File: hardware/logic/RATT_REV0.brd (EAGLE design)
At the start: 109.3 x 76.2 mm, 104 parts, among them J1 0472192001, J2 F-1X02-SIP-100-40, J3 F-1X06-SIP-100-40, J4 F-1X07-SIP-100-40, J5 F-1X02-SIP-100-40, J6 F-1X05-SIP-100-40, Q1 2.5A/30V, Q2 MBT3904DW1T1, Q5 2N7002, U1 ESP-WROOM-32, U3 MCP73831, U4 FT231XS, U5 AP2112K-3.3V, U6 PCA9539PW

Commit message: Bye bye ESP, hello pi
Removed all the old ESP stuff, added some power path stuff, conencted nets to the pi pins renaming as needed.  Mucho cleanup needed.
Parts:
- removed C11, C14, C16: 0.1uF, SparkFun-Capacitors:0603
- removed C12, C13: 47pF, SparkFun-Capacitors:0603
- removed C15: 4.7uF, SparkFun-Capacitors:0603-CAP
- removed C4: 0.1uF, SparkFun-Passives:0603-CAP
- removed D2: BAT20J, SparkFun-DiscreteSemi:SOD-323
- removed J1: 0472192001, DURRIDGE:USD
- removed J2: F-1X02-SIP-100-40, con-headers-jp:SIP-100-02-40
- removed J6: F-1X05-SIP-100-40, con-headers-jp:SIP-100-05-40
- removed JP15: (no value), SparkFun-Connectors:USB-B-MICRO-SMD_V03
- removed R13, R14: 51K, SparkFun-Passives:0603-RES
- removed R15, R16: 27, SparkFun-Resistors:0603
- removed R2, R3, R4: 100R, SparkFun-Resistors:0603-RES
- removed R22, R23: 10k, SparkFun-Resistors:0603
- removed SW4: (no value), MakeIt_Labs:ESWITCH320
- removed U1: ESP-WROOM-32, esp32:ESP-WROOM-32
- removed U4: FT231XS, SparkFun-DigitalIC:SSOP20_L
- added Q3, Q6: 2.5A/30V, SparkFun-DiscreteSemi:SOT23-3
- added Q4, Q7: (no value), DURRIDGE-TRANSISTORS:SOT23-3
- added R36: 1K, SparkFun-Resistors:0603
- added SW0: (no value), MakeIt_Labs:ESWITCH320
- R1: value 100R -> 0R; device SparkFun-Resistors:0603-RES -> SparkFun-Passives:0603-RES
- R10, R11: value 51K -> 10k; device SparkFun-Passives:0603-RES -> SparkFun-Resistors:0603
- R12, R9: value 51K -> 1k; device SparkFun-Passives:0603-RES -> SparkFun-Resistors:0603
- moved R1 473.9 mm to (-173.7, -204.2)
- moved R9 471.8 mm to (-173.7, -197.9)
- moved R10 470.3 mm to (-173.7, -201.2)
- moved R12 455.2 mm to (-167.6, -194.6)
- moved R11 454.1 mm to (-164.6, -191.3)
- moved SW2 12.7 mm to (80.6, 31.8)
- moved SW3 12.7 mm to (80.6, 19.1)
- moved SW1 12.7 mm to (80.6, 44.5)
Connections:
- removed net 3.3V_F: C16.1, U4.13, U4.14, U4.3
- removed net BOOTLOADER: Q2.6, U1.25
- removed net D+: C13.1, JP15.D+, R16.1
- removed net D-: C12.1, JP15.D-, R15.1
- removed net DTR: J6.4, Q2.1, R22.1, U4.1
- removed net N$13: Q2.5, R22.2
- removed net N$15: Q2.2, R23.2
- removed net N$19: R25.1, U6.1
- removed net N$20: R32.1, SW2.3, U1.5
- removed net N$23: R33.1, SW3.3, U1.6
- removed net N$24: R34.1, SW4.3, U1.7
- removed net N$25: R31.1, SW1.3, U1.4
- removed net RFID_RXD: U1.27
- removed net RTS: J6.5, Q2.4, R23.1, U4.2
- removed net RXD0: J6.3, U1.34, U4.20
- removed net SD_CLK: J1.5, R1.2, R14.2, U1.13
- removed net SD_CMD: J1.3, R10.1, R4.2, U1.23
- removed net SD_D0: J1.7, R11.1, U1.24
- removed net SD_D1: J1.8, R13.1, U1.26
- removed net SD_D2: J1.1, R12.1, R2.2, U1.14
- removed net SD_D3: J1.2, R3.2, R9.1, U1.16
- removed net SPI_MISO: SJ10.2, U1.31
- removed net SPI_MOSI: SJ8.2, U1.37
- removed net SPI_SCK: SJ9.2, U1.30
- removed net SPI_TFT_CS0: SJ7.2, U1.29
- removed net TFT_BACKLIGHT: SJ11.2, U1.9
- removed net TFT_DAT/COM: SJ6.2, U1.12
- removed net TFT_RESET: R30.1, SJ5.2, U1.8, U6.3
- removed net TXD0: J6.2, U1.35, U4.4
- new net !BUTTON0: R31.1, SW0.3, U$1.31
- new net !BUTTON1: R32.1, SW1.3, U$1.26
- new net !BUTTON2: R33.1, SW2.3, U$1.32
- new net !BUTTON3: R34.1, SW3.3, U$1.33
- new net !I/O_IRQ: R25.1, U$1.7, U6.1
- new net !I/O_RESET: R30.1, U6.3
- new net !LED0: U$1.29
- new net !SHUTDOWN: R12.1, U$1.13
- new net +5V: C19.1, Q1.1, Q6.3, R17.2, R18.1, R9.2, U3.4
- new net 3V3@2: R1.1, U$1.1, U$1.17
- new net CHARGE_STATUS: D1.C, R36.2, U3.1
- new net GND@3: U$1.25, U$1.39, U$1.9
- new net GND@6: U$1.14, U$1.20, U$1.30, U$1.34, U$1.6
- new net LCD_BACKLIGHT: SJ11.2, U$1.16
- new net LCD_CS: SJ7.2, U$1.24
- new net LCD_D/C: SJ6.2, U$1.18
- new net LCD_MISO: SJ10.2, U$1.21
- new net LCD_MOSI: SJ8.2, U$1.19
- new net LCD_RESET: SJ5.2, U$1.22
- new net LCD_SCK: SJ9.2, U$1.23
- new net N$35: Q7.1, R9.1
- new net N$36: U$1.36
- new net N$37: Q3.1, Q4.3, R11.1
- new net N$38: Q4.1, R12.2
- new net N$39: U$1.15
- new net N$40: U$1.11
- new net PWR_LOSS: U$1.37
- net +3V3: now also R1.2; no longer C1.1, C17.1, C2.1, C4.1, C9.1, J1.4, R10.2, R11.2, R12.2, R13.2, R5.2, R7.2, R9.2, U1.2, U2.7, U2.8
- net 3.3V: now also R36.1
- net GND: now also Q4.2, Q7.2, SW0.1; no longer C1.2, C11.2, C12.2, C13.2, C14.2, C15.2, C16.2, C4.2, J1.6, J1.G1, J1.G2, J1.G3, J1.G4, J2.2, J6.1, JP15.GND, JP15.SHIELD1, JP15.SHIELD2, JP15.SHIELD3, R14.1, SW4.1, U1.1, U1.15, U1.38, U1.GND, U4.16, U4.6
- net I2C_SCL: now also U$1.5; no longer U1.36
- net I2C_SDA: now also U$1.3; no longer U1.33
- net I2S_BCK: now also U$1.12; no longer U1.11
- net I2S_DOUT: now also U$1.40; no longer U1.28
- net I2S_WS/LRCLK: now also U$1.35; no longer U1.10
- net JTAG_TCK: no longer R3.1
- net JTAG_TDI: no longer R2.1
- net JTAG_TDO: no longer R4.1
- net JTAG_TMS: no longer R1.1
- net N$10: now also Q1.3, Q3.3; no longer D1.C, U3.1
- net N$8: now also C2.1, R5.2; no longer R15.2, U4.12
- net N$9: now also Q6.1, Q7.3, R10.2; no longer R16.2, U4.11
- net RFID_RX: now also U$1.10
- net RFID_TX: now also U$1.8
- net VIN: now also C17.1, C9.1, Q6.2, R10.1, R7.2, U$1.2, U$1.4, U2.7, U2.8; no longer D2.C
- net VUSB-RAW: no longer C11.1, J2.1, JP15.VBUS
- net V_BATT: now also Q3.2, R11.2; no longer Q1.3
- net V_USB: no longer C14.1, C15.1, C19.1, D2.A, Q1.1, R17.2, R18.1, U3.4, U4.15
- net ~RESET: no longer Q2.3, R5.1, U1.3
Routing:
- net SD_CLK: track 32.5 -> 0.00 mm
- net SD_D1: track 26.5 -> 0.00 mm
- net SD_D2: track 21.0 -> 0.00 mm
- net SD_CMD: track 18.8 -> 0.00 mm
- net SD_D3: track 17.7 -> 0.00 mm
- net SD_D0: track 17.5 -> 0.00 mm
- net N$8: track 14.4 -> 0.00 mm
- net N$9: track 10.7 -> 0.00 mm
- net 3.3V_F: track 8.49 -> 0.00 mm
- net RXD0: track 8.48 -> 0.00 mm
- net +3V3: track 9.02 -> 1.52 mm
- net D+: track 5.82 -> 0.00 mm
- net D-: track 5.23 -> 0.00 mm
- net VIN: track 0.00 -> 5.23 mm
- net RTS: track 3.46 -> 0.00 mm
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
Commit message: Forgot to save first
derp
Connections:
- removed net N$40: U$1.11
- net !I/O_RESET: now also U$1.11
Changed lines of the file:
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@@
 <contactref element="U$1" pad="15"/>
-</signal>
-<signal name="N$40">
-<contactref element="U$1" pad="11"/>
 </signal>
 <signal name="!I/O_IRQ">
@@
 <contactref element="U6" pad="3"/>
 <contactref element="R30" pad="1"/>
+<contactref element="U$1" pad="11"/>
 <wire x1="-95.592" y1="-82.55" x2="-111.887" y2="-68.8086" width="0" layer="19" extent="1-1"/>
+<wire x1="-14.394" y1="38.366" x2="-111.887" y2="-68.8086" width="0" layer="19" extent="1-1"/>
 </signal>
 </signals>

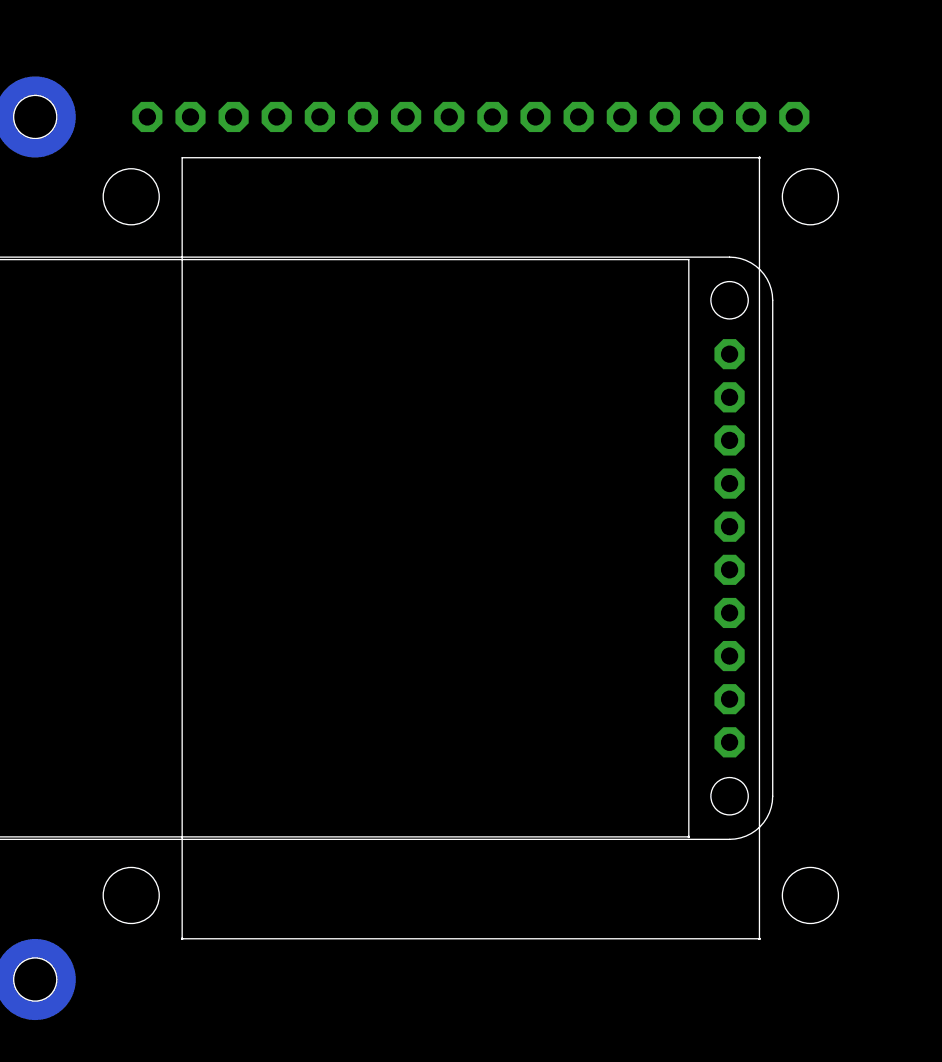
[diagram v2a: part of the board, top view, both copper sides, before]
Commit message: new display, buttons moved
Added chinafruit 2.0, moved buttons to i/o expander, added i/o lines to expander
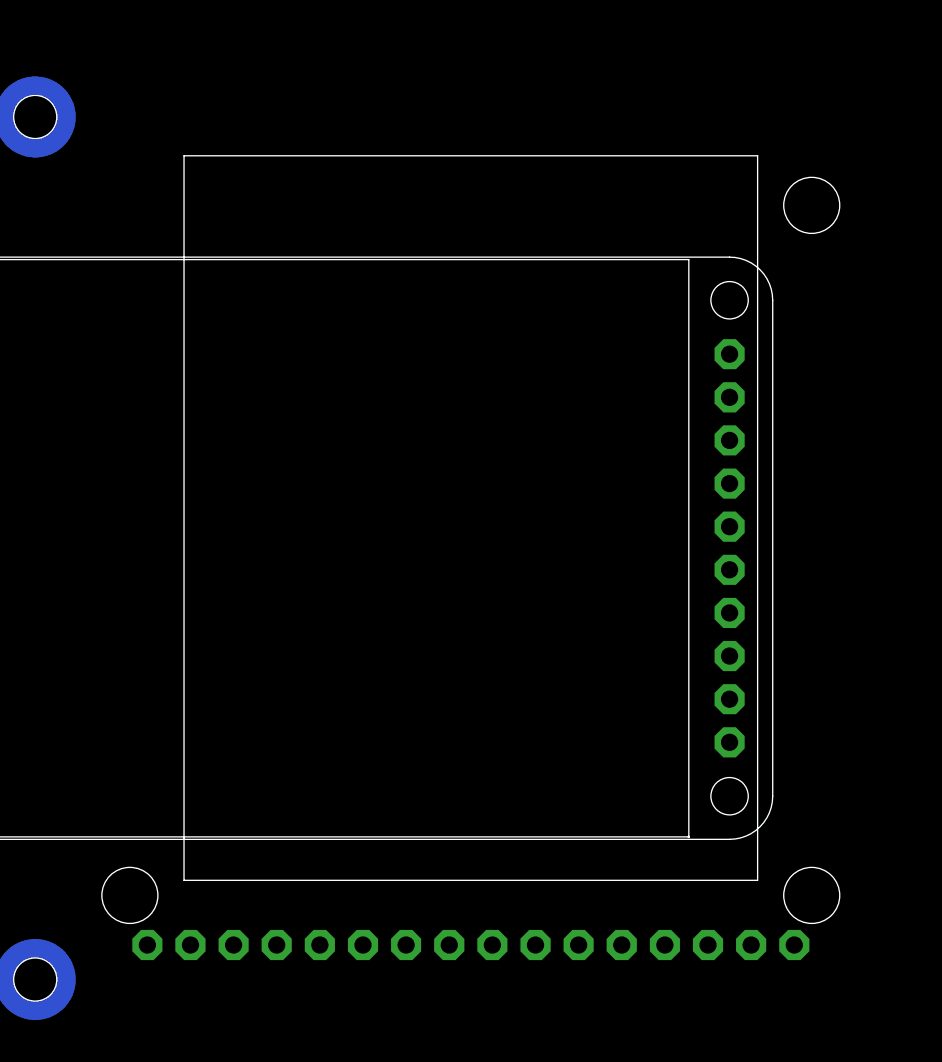
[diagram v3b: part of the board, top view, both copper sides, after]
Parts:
- removed LCD2: 1.8TFT_CHI, MakeIt_Labs:1.8TFT_CHI
- added LCD3: 1.8TFT_CHI2.0, MakeIt_Labs:1.8TFT_CHI_2.0
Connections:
- removed net N$36: U$1.36
- removed net N$39: U$1.15
- new net IN0: U6.4
- new net IN1: U6.5
- new net IN2: U6.6
- new net IN3: U6.7
- new net N$13: U$1.26
- new net OUT0: U6.8
- new net OUT1: U6.9
- new net OUT2: U6.10
- new net OUT3: U6.11
- net !BUTTON0: now also U6.13; no longer U$1.31
- net !BUTTON1: now also U6.14; no longer U$1.26
- net !BUTTON2: now also U6.15; no longer U$1.32
- net !BUTTON3: now also U6.16; no longer U$1.33
- net N$26: now also LCD3.15, LCD3.2; no longer LCD2.15, LCD2.2
- net N$27: now also LCD3.6; no longer LCD2.6
- net N$28: now also LCD3.7; no longer LCD2.7
- net N$29: now also LCD3.10; no longer LCD2.10
- net N$3: now also LCD3.1; no longer LCD2.1
- net N$30: now also LCD3.8; no longer LCD2.8
- net N$31: now also LCD3.9; no longer LCD2.9
- net N$34: now also LCD3.16; no longer LCD2.16
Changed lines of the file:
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@@
 <element name="SJ10" library="SparkFun-Passives" package="PAD-JUMPER-2-NC_BY_TRACE_YES_SILK" value="JUMPER-PAD-2-NC_BY_TRACE" x="-149.8" y="-133.32"/>
 <element name="SJ11" library="SparkFun-Passives" package="PAD-JUMPER-2-NC_BY_TRACE_YES_SILK" value="JUMPER-PAD-2-NC_BY_TRACE" x="-125.9" y="-129.06" rot="R180"/>
-<element name="LCD2" library="MakeIt_Labs" package="1.8TFT_CHI" value="1.8TFT_CHI" x="40.64" y="38.1" rot="MR270"/>
 <element name="J4" library="con-headers-jp" package="SIP-100-07-40" value="F-1X07-SIP-100-40" x="-139.7" y="-144.78"/>
 <element name="C24" library="SparkFun-Capacitors" package="0603-CAP@1" value="0.1uF" x="-152.4" y="-157.48"/>
@@
 </element>
 <element name="R1" library="SparkFun-Passives" package="0603-RES" value="0R" x="-173.736" y="-204.216"/>
+<element name="LCD3" library="MakeIt_Labs" package="1.8TFT_CHI_2.0" value="1.8TFT_CHI2.0" x="40.64" y="14.732" rot="MR90"/>
 </elements>
 <signals>
@@
 <contactref element="SJ3" pad="1"/>
 <contactref element="LCD1" pad="1"/>
-<contactref element="LCD2" pad="1"/>
-<wire x1="59.69" y1="63.5" x2="55.88" y2="49.53" width="0" layer="19" extent="1-1"/>
-<wire x1="-142.708" y1="-118.02" x2="59.69" y2="63.5" width="0" layer="19" extent="1-1"/>
+<contactref element="LCD3" pad="1"/>
+<wire x1="21.59" y1="14.732" x2="55.88" y2="49.53" width="0" layer="19" extent="1-1"/>
+<wire x1="-142.708" y1="-118.02" x2="21.59" y2="14.732" width="0" layer="19" extent="1-1"/>
 </signal>
 <signal name="N$26">
 <contactref element="SJ4" pad="1"/>
 <contactref element="LCD1" pad="2"/>
-<contactref element="LCD2" pad="2"/>
-<contactref element="LCD2" pad="15"/>
-<wire x1="55.88" y1="46.99" x2="24.13" y2="63.5" width="0" layer="19" extent="1-1"/>
-<wire x1="57.15" y1="63.5" x2="55.88" y2="46.99" width="0" layer="19" extent="1-1"/>
-<wire x1="-132.908" y1="-133.32" x2="57.15" y2="63.5" width="0" layer="19" extent="1-1"/>
+<contactref element="LCD3" pad="2"/>
+<contactref element="LCD3" pad="15"/>
+<wire x1="57.15" y1="14.732" x2="55.88" y2="46.99" width="0" layer="19" extent="1-1"/>
+<wire x1="24.13" y1="14.732" x2="57.15" y2="14.732" width="0" layer="19" extent="1-1"/>
+<wire x1="-132.908" y1="-133.32" x2="24.13" y2="14.732" width="0" layer="19" extent="1-1"/>
 </signal>
 <signal name="N$27">
 <contactref element="SJ5" pad="1"/>
 <contactref element="LCD1" pad="3"/>
-<contactref element="LCD2" pad="6"/>
-<wire x1="46.99" y1="63.5" x2="55.88" y2="44.45" width="0" layer="19" extent="1-1"/>
-<wire x1="-135.808" y1="-133.32" x2="46.99" y2="63.5" width="0" layer="19" extent="1-1"/>
+<contactref element="LCD3" pad="6"/>
+<wire x1="34.29" y1="14.732" x2="55.88" y2="44.45" width="0" layer="19" extent="1-1"/>
+<wire x1="-135.808" y1="-133.32" x2="34.29" y2="14.732" width="0" layer="19" extent="1-1"/>
 </signal>
 <signal name="N$28">
 <contactref element="SJ6" pad="1"/>
 <contactref element="LCD1" pad="4"/>
-<contactref element="LCD2" pad="7"/>
-<wire x1="55.88" y1="41.91" x2="44.45" y2="63.5" width="0" layer="19" extent="1-1"/>
-<wire x1="-138.708" y1="-133.32" x2="55.88" y2="41.91" width="0" layer="19" extent="1-1"/>
+<contactref element="LCD3" pad="7"/>
+<wire x1="36.83" y1="14.732" x2="55.88" y2="41.91" width="0" layer="19" extent="1-1"/>
+<wire x1="-138.708" y1="-133.32" x2="36.83" y2="14.732" width="0" layer="19" extent="1-1"/>
 </signal>
 <signal name="N$29">
 <contactref element="SJ7" pad="1"/>
 <contactref element="LCD1" pad="6"/>
-<contactref element="LCD2" pad="10"/>
-<wire x1="55.88" y1="36.83" x2="36.83" y2="63.5" width="0" layer="19" extent="1-1"/>
-<wire x1="-141.608" y1="-133.32" x2="55.88" y2="36.83" width="0" layer="19" extent="1-1"/>
+<contactref element="LCD3" pad="10"/>
+<wire x1="44.45" y1="14.732" x2="55.88" y2="36.83" width="0" layer="19" extent="1-1"/>
+<wire x1="-141.608" y1="-133.32" x2="44.45" y2="14.732" width="0" layer="19" extent="1-1"/>
 </signal>
 <signal name="N$30">
 <contactref element="SJ8" pad="1"/>
 <contactref element="LCD1" pad="7"/>
-<contactref element="LCD2" pad="8"/>
-<wire x1="55.88" y1="34.29" x2="41.91" y2="63.5" width="0" layer="19" extent="1-1"/>
-<wire x1="-144.508" y1="-133.32" x2="55.88" y2="34.29" width="0" layer="19" extent="1-1"/>
+<contactref element="LCD3" pad="8"/>
+<wire x1="39.37" y1="14.732" x2="55.88" y2="34.29" width="0" layer="19" extent="1-1"/>
+<wire x1="-144.508" y1="-133.32" x2="39.37" y2="14.732" width="0" layer="19" extent="1-1"/>
 </signal>
 <signal name="N$31">
 <contactref element="SJ9" pad="1"/>
 <contactref element="LCD1" pad="8"/>
-<contactref element="LCD2" pad="9"/>
-<wire x1="55.88" y1="31.75" x2="39.37" y2="63.5" width="0" layer="19" extent="1-1"/>
-<wire x1="-147.408" y1="-133.32" x2="55.88" y2="31.75" width="0" layer="19" extent="1-1"/>
+<contactref element="LCD3" pad="9"/>
+<wire x1="41.91" y1="14.732" x2="55.88" y2="31.75" width="0" layer="19" extent="1-1"/>
+<wire x1="-147.408" y1="-133.32" x2="41.91" y2="14.732" width="0" layer="19" extent="1-1"/>
 </signal>
 <signal name="N$32">
@@
 </signal>
 <signal name="N$34">
-<contactref element="LCD2" pad="16"/>
 <contactref element="Q5" pad="1"/>
-<wire x1="-152.3746" y1="-173.736" x2="21.59" y2="63.5" width="0" layer="19" extent="1-1"/>
+<contactref element="LCD3" pad="16"/>
+<wire x1="-152.3746" y1="-173.736" x2="59.69" y2="14.732" width="0" layer="19" extent="1-1"/>
 </signal>
 <signal name="N$8">
@@
 <contactref element="U$1" pad="37"/>
 </signal>
-<signal name="N$36">
-<contactref element="U$1" pad="36"/>
-</signal>
 <signal name="!BUTTON3">
-<contactref element="U$1" pad="33"/>
 <contactref element="R34" pad="1"/>
 <contactref element="SW3" pad="3"/>
-<wire x1="-14.394" y1="10.426" x2="-113.45" y2="-136.1" width="0" layer="19" extent="1-1"/>
-<wire x1="79.375" y1="17.78" x2="-14.394" y2="10.426" width="0" layer="19" extent="1-1"/>
+<contactref element="U6" pad="16"/>
+<wire x1="-106.045" y1="-72.7202" x2="-113.45" y2="-136.1" width="0" layer="19" extent="1-1"/>
+<wire x1="79.375" y1="17.78" x2="-106.045" y2="-72.7202" width="0" layer="19" extent="1-1"/>
 </signal>
 <signal name="!BUTTON2">
-<contactref element="U$1" pad="32"/>
 <contactref element="R33" pad="1"/>
 <contactref element="SW2" pad="3"/>
-<wire x1="-11.854" y1="12.966" x2="-113.45" y2="-133.1" width="0" layer="19" extent="1-1"/>
-<wire x1="79.375" y1="30.48" x2="-11.854" y2="12.966" width="0" layer="19" extent="1-1"/>
+<contactref element="U6" pad="15"/>
+<wire x1="-106.045" y1="-73.3806" x2="-113.45" y2="-133.1" width="0" layer="19" extent="1-1"/>
+<wire x1="79.375" y1="30.48" x2="-106.045" y2="-73.3806" width="0" layer="19" extent="1-1"/>
 </signal>
 <signal name="!BUTTON0">
-<contactref element="U$1" pad="31"/>
 <contactref element="R31" pad="1"/>
 <contactref element="SW0" pad="3"/>
-<wire x1="-14.394" y1="12.966" x2="-113.45" y2="-127.1" width="0" layer="19" extent="1-1"/>
-<wire x1="79.375" y1="55.88" x2="-14.394" y2="12.966" width="0" layer="19" extent="1-1"/>
+<contactref element="U6" pad="13"/>
+<wire x1="-106.045" y1="-74.676" x2="-113.45" y2="-127.1" width="0" layer="19" extent="1-1"/>
+<wire x1="79.375" y1="55.88" x2="-106.045" y2="-74.676" width="0" layer="19" extent="1-1"/>
 </signal>
 <signal name="!LED0">
@@
 </signal>
 <signal name="!BUTTON1">
-<contactref element="U$1" pad="26"/>
 <contactref element="R32" pad="1"/>
 <contactref element="SW1" pad="3"/>
-<wire x1="-11.854" y1="20.586" x2="-113.45" y2="-130.1" width="0" layer="19" extent="1-1"/>
-<wire x1="79.375" y1="43.18" x2="-11.854" y2="20.586" width="0" layer="19" extent="1-1"/>
-</signal>
-<signal name="N$39">
-<contactref element="U$1" pad="15"/>
+<contactref element="U6" pad="14"/>
+<wire x1="-106.045" y1="-74.0156" x2="-113.45" y2="-130.1" width="0" layer="19" extent="1-1"/>
+<wire x1="79.375" y1="43.18" x2="-106.045" y2="-74.0156" width="0" layer="19" extent="1-1"/>
 </signal>
 <signal name="!I/O_IRQ">
@@
 <wire x1="-14.394" y1="38.366" x2="-111.887" y2="-68.8086" width="0" layer="19" extent="1-1"/>
 </signal>
+<signal name="IN0">
+<contactref element="U6" pad="4"/>
+</signal>
+<signal name="IN1">
+<contactref element="U6" pad="5"/>
+</signal>
+<signal name="IN2">
+<contactref element="U6" pad="6"/>
+</signal>
+<signal name="IN3">
+<contactref element="U6" pad="7"/>
+</signal>
+<signal name="OUT0">
+<contactref element="U6" pad="8"/>
+</signal>
+<signal name="OUT1">
+<contactref element="U6" pad="9"/>
+</signal>
+<signal name="OUT2">
+<contactref element="U6" pad="10"/>
+</signal>
+<signal name="OUT3">
+<contactref element="U6" pad="11"/>
+</signal>
+<signal name="N$13">
+<contactref element="U$1" pad="26"/>
+</signal>
 </signals>
